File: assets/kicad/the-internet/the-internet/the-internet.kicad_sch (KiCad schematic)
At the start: 34 parts, among them J1 LED connector, J2 Battery, Q1 IRF9240, Q2 BC547, Q3 BC547, Q4 BC547, Q6 BC557, Q7 BC557, Q8 BC547, SW1 NO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

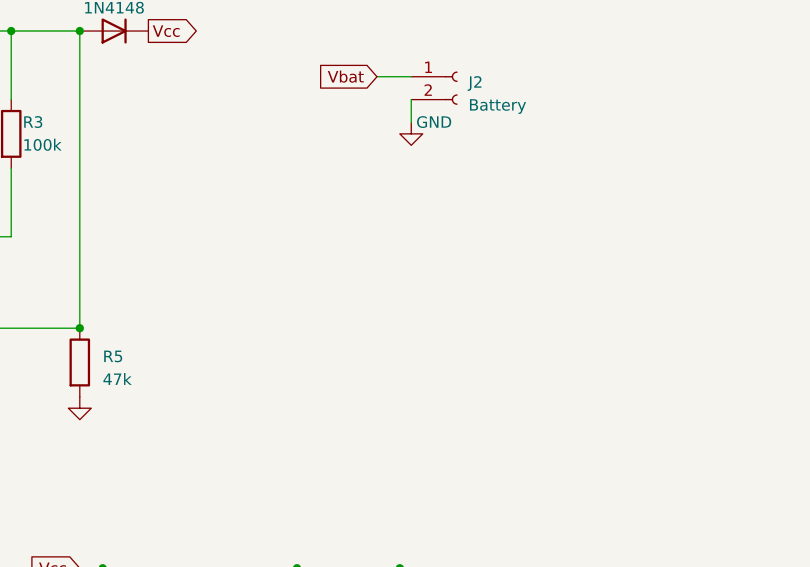
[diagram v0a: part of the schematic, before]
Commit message: Added signal terminal
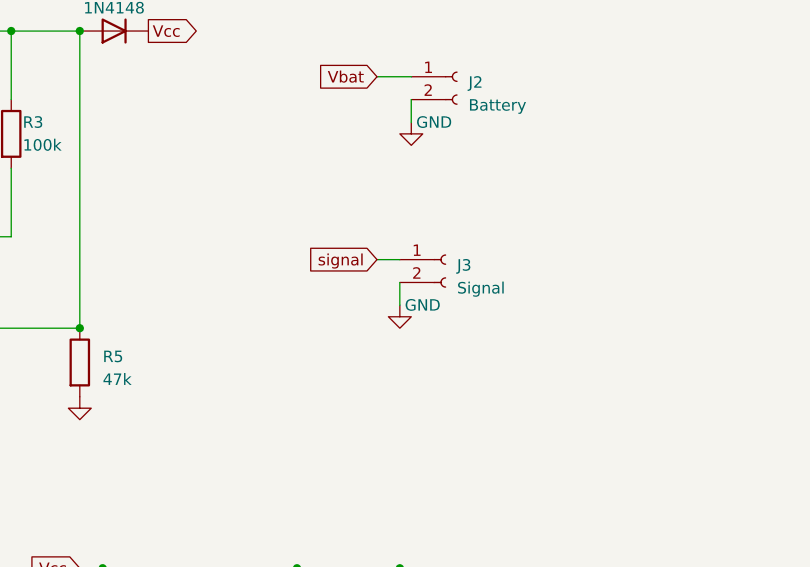
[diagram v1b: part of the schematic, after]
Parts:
- added J3: Signal, Connector_PinHeader_2.54mm:PinHeader_1x02_P2.54mm_Vertical, symbol Connector:Conn_01x02_Socket
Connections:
- net GND: now also J3.2 (Pin_2)
- net signal: now also J3.1 (Pin_1)
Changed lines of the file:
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@@
+    (stroke (width 0) (type default))
+  )
+  (wire (pts (xy 95.25 55.88) (xy 97.79 55.88))
     (stroke (width 0) (type default))
   )
@@
   )
   (wire (pts (xy 81.28 107.95) (xy 86.36 107.95))
+    (stroke (width 0) (type default))
+  )
+  (wire (pts (xy 97.79 58.42) (xy 97.79 60.96))
     (stroke (width 0) (type default))
   )
@@
     )
   )
+  (global_label "signal" (shape input) (at 95.25 55.88 180) (fields_autoplaced)
+    (effects (font (size 1.27 1.27)) (justify right))
+    (property "Intersheetrefs" "${INTERSHEET_REFS}" (at 86.5991 55.88 0)
+      (effects (font (size 1.27 1.27)) (justify right) hide)
+    )
+  )
   (global_label "signal" (shape output) (at 194.31 81.28 0) (fields_autoplaced)
     (effects (font (size 1.27 1.27)) (justify left))
@@
     )
   )
+  (symbol (lib_id "Connector:Conn_01x02_Socket") (at 102.87 55.88 0) (unit 1)
+    (in_bom yes) (on_board yes) (dnp no) (fields_autoplaced)
+    (property "Reference" "J3" (at 104.14 56.515 0)
+      (effects (font (size 1.27 1.27)) (justify left))
+    )
+    (property "Value" "Signal" (at 104.14 59.055 0)
+      (effects (font (size 1.27 1.27)) (justify left))
+    )
+    (property "Footprint" "Connector_PinHeader_2.54mm:PinHeader_1x02_P2.54mm_Vertical" (at 102.87 55.88 0)
+      (effects (font (size 1.27 1.27)) hide)
+    )
+    (property "Datasheet" "~" (at 102.87 55.88 0)
+      (effects (font (size 1.27 1.27)) hide)
+    )
+    (pin "1")
+    (pin "2")
+    (instances
+      (project "the-internet"
+        (path "/aa7118a6-a457-43b0-8d93-850b87ec5f8a"
+          (reference "J3") (unit 1)
+        )
+      )
+    )
+  )
   (symbol (lib_id "Device:R") (at 40.64 46.99 90) (unit 1)
     (in_bom yes) (on_board yes) (dnp no) (fields_autoplaced)
@@
         )
       )
+    )
+  )
+  (symbol (lib_id "power:GND") (at 97.79 60.96 0) (unit 1)
+    (in_bom yes) (on_board yes) (dnp no)
+    (property "Reference" "#PWR08" (at 97.79 67.31 0)
+      (effects (font (size 1.27 1.27)) hide)
+    )
+    (property "Value" "GND" (at 100.33 60.96 0)
+      (effects (font (size 1.27 1.27)))
+    )
+    (property "Footprint" "" (at 97.79 60.96 0)
+      (effects (font (size 1.27 1.27)) hide)
+    )
+    (property "Datasheet" "" (at 97.79 60.96 0)
+      (effects (font (size 1.27 1.27)) hide)
+    )
+    (pin "1")
+    (instances
+      (project "the-internet"
+        (path "/aa7118a6-a457-43b0-8d93-850b87ec5f8a"
+          (reference "#PWR08") (unit 1)
+        )
+      )

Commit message: Added final version of the internet
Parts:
- R7: value 33k -> 68k
- R8: value 68k -> 33k
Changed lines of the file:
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@@
       (effects (font (size 1.27 1.27)) (justify left))
     )
-    (property "Value" "68k" (at 87.63 111.76 0)
+    (property "Value" "33k" (at 87.63 111.76 0)
       (effects (font (size 1.27 1.27)) (justify left))
     )
@@
       (effects (font (size 1.27 1.27)) (justify left))
     )
-    (property "Value" "33k" (at 77.47 113.03 0)
-      (effects (font (size 1.27 1.27)) (justify left))
-    )
+    (property "Value" "68k" (at 77.47 113.03 0)
+      (effects (font (size 1.27 1.27)) (justify left))
+    )
